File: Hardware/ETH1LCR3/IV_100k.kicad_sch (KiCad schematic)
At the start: 16 parts, among them Q901 BSS123, U1203 AQY221R2S, U901 AD8099ARDZ, U902 AQY221R2S

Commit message: PCB layout
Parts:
- C903: value DNP -> 1p; now fitted; now in the parts list
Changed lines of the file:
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@@
 		(unit 1)
 		(exclude_from_sim no)
-		(in_bom no)
+		(in_bom yes)
 		(on_board yes)
-		(dnp yes)
+		(dnp no)
 		(fields_autoplaced yes)
 		(property "Reference" "C903"
@@
 			)
 		)
-		(property "Value" "DNP"
+		(property "Value" "1p"
 			(at 143.51 63.5 90)
 			(effects

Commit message: PCB layout
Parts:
- added Q1202: MMBT3904, Package_TO_SOT_SMD:SOT-23, symbol Transistor_BJT:MMBT3904
- added R1207: 10k, Resistor_SMD:R_0603_1608Metric_Pad0.98x0.95mm_HandSolder, symbol Device:R
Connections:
- net GND: now also Q1202.2 (E)
- net SW4: now also R1207.2; no longer R903.1, U1203.2
- new net: Q1202.1 (B), R1207.1
- new net _SW4: Q1202.3 (C), R903.1, U1203.2
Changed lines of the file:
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@@
 		)
 	)
-	(label "SW4"
+	(label "_SW4"
 		(at 208.28 85.09 0)
 		(fields_autoplaced yes)
@@
 		)
 	)
-	(label "SW4"
+	(label "_SW4"
 		(at 111.76 111.76 0)
 		(fields_autoplaced yes)
@@
 	(hierarchical_label "SW4"
 		(shape input)
-		(at 215.9 85.09 0)
+		(at 220.98 69.85 90)
 		(fields_autoplaced yes)
 		(effects
@@
 	)
 	(symbol
+		(lib_id "Device:R")
+		(at 220.98 73.66 180)
+		(unit 1)
+		(exclude_from_sim no)
+		(in_bom yes)
+		(on_board yes)
+		(dnp no)
+		(property "Reference" "R1207"
+			(at 215.9 73.66 90)
+			(effects
+				(font
+					(size 1.27 1.27)
+				)
+			)
+		)
+		(property "Value" "10k"
+			(at 218.44 73.66 90)
+			(effects
+				(font
+					(size 1.27 1.27)
+				)
+			)
+		)
+		(property "Footprint" "Resistor_SMD:R_0603_1608Metric_Pad0.98x0.95mm_HandSolder"
+			(at 222.758 73.66 90)
+			(effects
+				(font
+					(size 1.27 1.27)
+				)
+				(hide yes)
+			)
+		)
+		(property "Datasheet" "~"
+			(at 220.98 73.66 0)
+			(effects
+				(font
+					(size 1.27 1.27)
+				)
+				(hide yes)
+			)
+		)
+		(property "Description" "Resistor"
+			(at 220.98 73.66 0)
+			(effects
+				(font
+					(size 1.27 1.27)
+				)
+				(hide yes)
+			)
+		)
+		(pin "1"
+		)
+		(pin "2"
+		)
+		(instances
+			(project "ETH1LCR3"
+				(path "/6623bacb-57aa-43ce-9e51-b38a560dd9fc/37965f22-1055-43ab-ab57-7d9b27fac2d0/3e63d325-b751-4193-9f6f-1795fa7b594f"
+					(reference "R1207")
+					(unit 1)
+				)
+			)
+		)
+	)
+	(symbol
 		(lib_id "power:GND")
 		(at 170.18 68.58 90)
@@
 	(symbol
 		(lib_id "power:GND")
+		(at 226.06 85.09 90)
+		(unit 1)
+		(exclude_from_sim no)
+		(in_bom yes)
+		(on_board yes)
+		(dnp no)
+		(fields_autoplaced yes)
+		(property "Reference" "#PWR01214"
+			(at 232.41 85.09 0)
+			(effects
+				(font
+					(size 1.27 1.27)
+				)
+				(hide yes)
+			)
+		)
+		(property "Value" "GND"
+			(at 229.87 85.0899 90)
+			(effects
+				(font
+					(size 1.27 1.27)
+				)
+				(justify right)
+			)
+		)
+		(property "Footprint" ""
+			(at 226.06 85.09 0)
+			(effects
+				(font
+					(size 1.27 1.27)
+				)
+				(hide yes)
+			)
+		)
+		(property "Datasheet" ""
+			(at 226.06 85.09 0)
+			(effects
+				(font
+					(size 1.27 1.27)
+				)
+				(hide yes)
+			)
+		)
+		(property "Description" "Power symbol creates a global label with name \"GND\" , ground"
+			(at 226.06 85.09 0)
+			(effects
+				(font
+					(size 1.27 1.27)
+				)
+				(hide yes)
+			)
+		)
+		(pin "1"
+		)
+		(instances
+			(project "ETH1LCR3"
+				(path "/6623bacb-57aa-43ce-9e51-b38a560dd9fc/37965f22-1055-43ab-ab57-7d9b27fac2d0/3e63d325-b751-4193-9f6f-1795fa7b594f"
+					(reference "#PWR01214")
+					(unit 1)
+				)
+			)
+		)
+	)
+	(symbol
+		(lib_id "power:GND")
 		(at 142.24 184.15 0)
 		(unit 1)
@@
 					(unit 1)
 				)
+			)
+		)
+	)
+	(symbol
+		(lib_id "Transistor_BJT:MMBT3904")
+		(at 220.98 82.55 90)
+		(mirror x)
+		(unit 1)
+		(exclude_from_sim no)
+		(in_bom yes)
+		(on_board yes)
+		(dnp no)
+		(property "Reference" "Q1202"
+			(at 227.584 77.216 90)
+			(effects
+				(font
+					(size 1.27 1.27)
+				)
+			)
+		)
+		(property "Value" "MMBT3904"
+			(at 227.584 79.756 90)
+			(effects
+				(font
+					(size 1.27 1.27)
+				)
+			)
+		)
+		(property "Footprint" "Package_TO_SOT_SMD:SOT-23"
+			(at 222.885 87.63 0)
+			(effects
+				(font
+					(size 1.27 1.27)
+					(italic yes)
+				)
+				(justify left)
+				(hide yes)
+			)
+		)
+		(property "Datasheet" "https://www.onsemi.com/pdf/datasheet/pzt3904-d.pdf"
+			(at 220.98 82.55 0)
+			(effects
+				(font
+					(size 1.27 1.27)
+				)
+				(justify left)
+				(hide yes)
+			)
+		)
+		(property "Description" "0.2A Ic, 40V Vce, Small Signal NPN Transistor, SOT-23"
+			(at 220.98 82.55 0)
+			(effects
+				(font
+					(size 1.27 1.27)
+				)
+				(hide yes)
+			)
+		)
+		(pin "3"
+		)
+		(pin "2"
+		)
+		(pin "1"
+		)
+		(instances
+			(project "ETH1LCR3"
+				(path "/6623bacb-57aa-43ce-9e51-b38a560dd9fc/37965f22-1055-43ab-ab57-7d9b27fac2d0/3e63d325-b751-4193-9f6f-1795fa7b594f"
+					(reference "Q1202")
+					(unit 1)
+				)

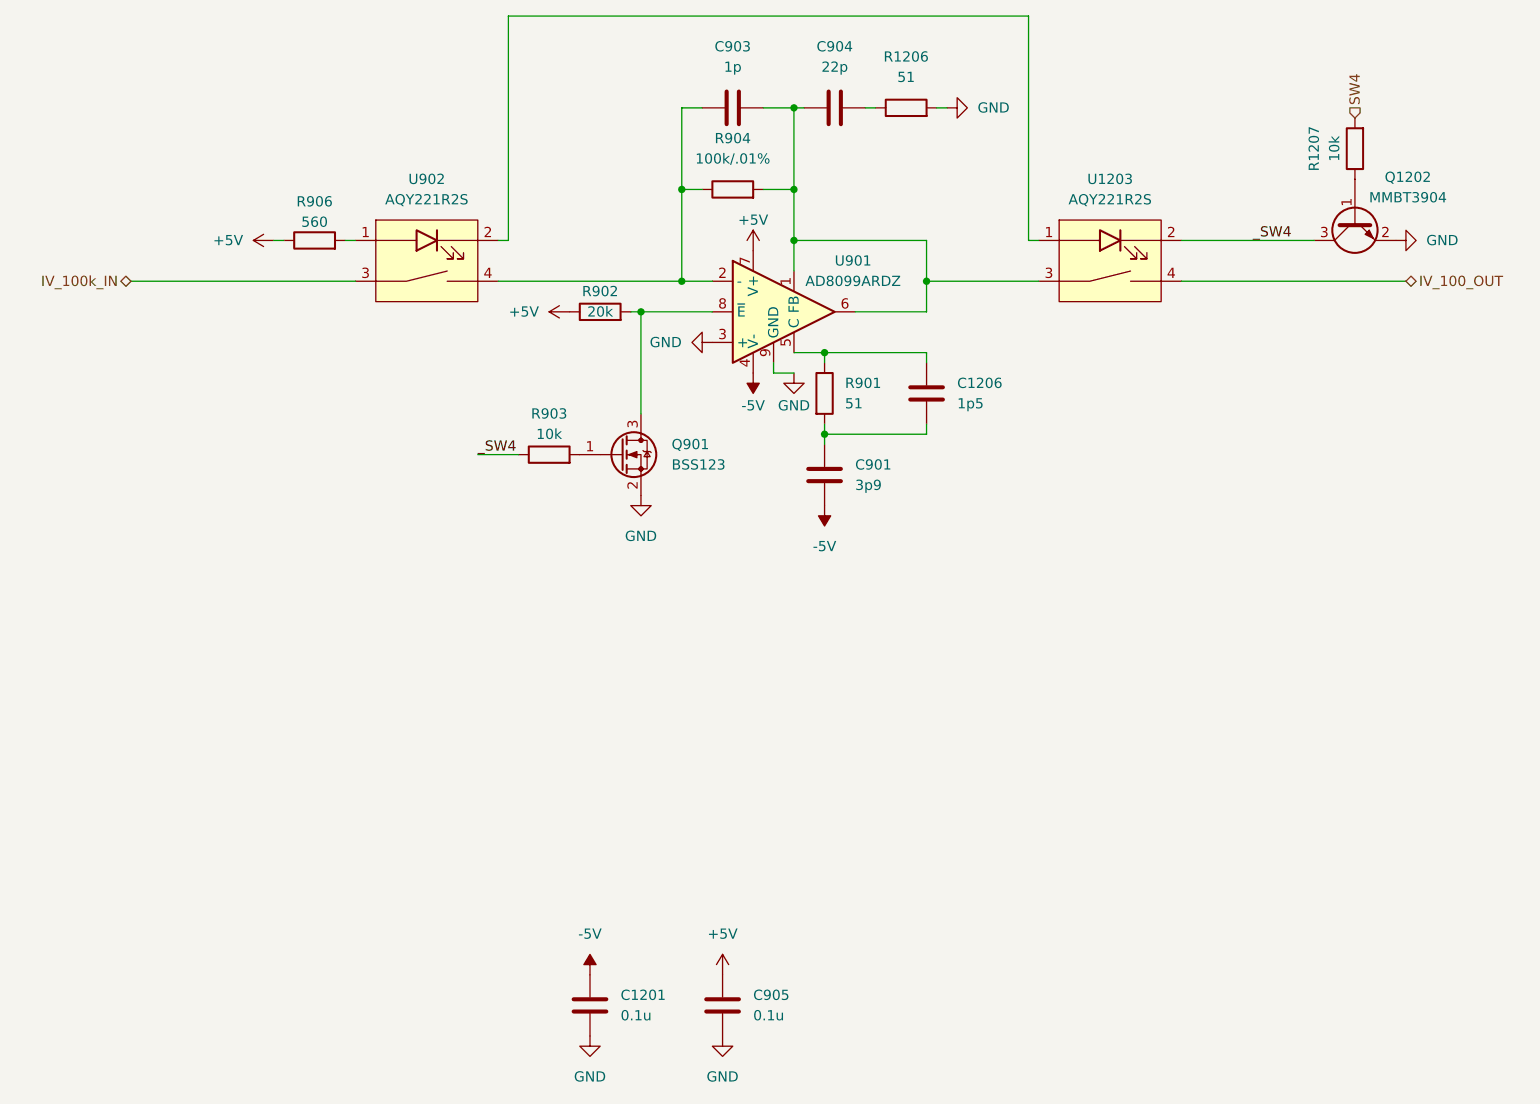
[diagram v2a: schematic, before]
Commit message: Updated project to KiCAD 9
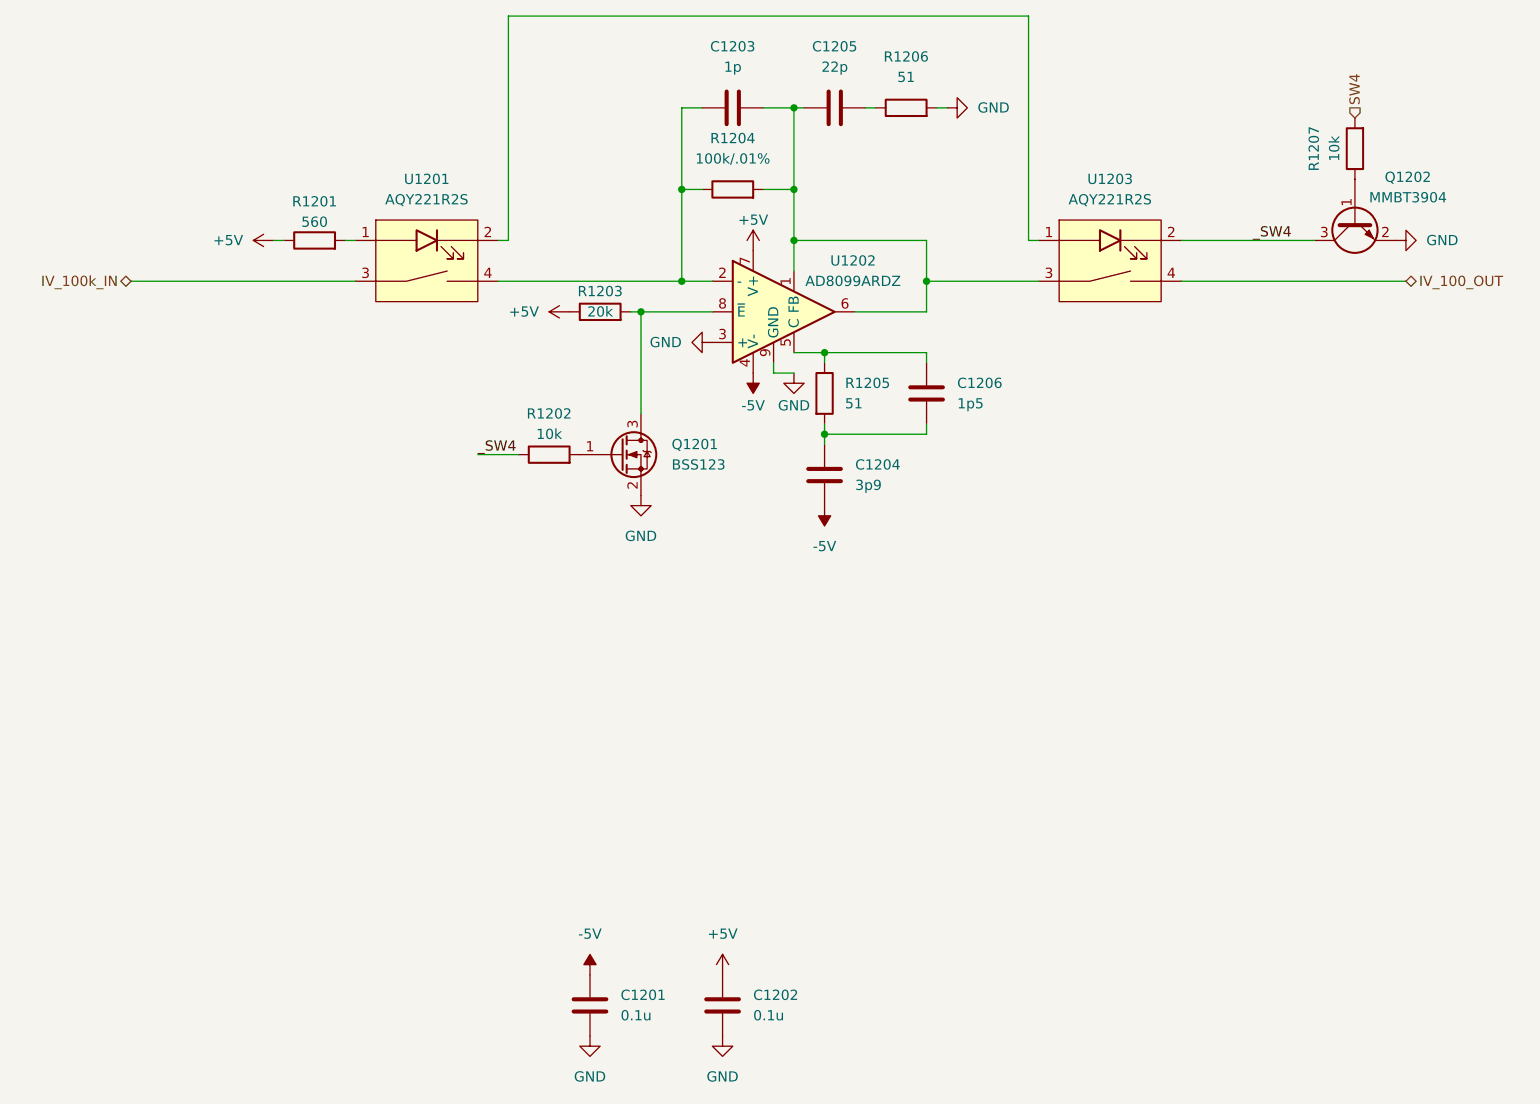
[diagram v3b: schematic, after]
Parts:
- renumbered C905 to C1202, C903 to C1203, C901 to C1204, C904 to C1205, Q901 to Q1201, R906 to R1201, R903 to R1202, R902 to R1203, R904 to R1204, R901 to R1205, U902 to U1201, U901 to U1202
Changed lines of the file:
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@@
 (kicad_sch
-	(version 20231120)
+	(version 20250114)
 	(generator "eeschema")
-	(generator_version "8.0")
+	(generator_version "9.0")
 	(paper "A4")
 	(junction
@@
 	(label "_SW4"
 		(at 208.28 85.09 0)
-		(fields_autoplaced yes)
 		(effects
 			(font
@@
 	(label "_SW4"
 		(at 111.76 111.76 0)
-		(fields_autoplaced yes)
 		(effects
 			(font
@@
 		(shape bidirectional)
 		(at 227.33 90.17 0)
-		(fields_autoplaced yes)
 		(effects
 			(font
@@
 		(shape input)
 		(at 220.98 69.85 90)
-		(fields_autoplaced yes)
 		(effects
 			(font
@@
 		(shape bidirectional)
 		(at 68.58 90.17 180)
-		(fields_autoplaced yes)
 		(effects
 			(font
@@
 		(dnp no)
 		(fields_autoplaced yes)
-		(property "Reference" "#PWR0904"
+		(property "Reference" "#PWR01202"
 			(at 127 93.98 0)
 			(effects
@@
 		(dnp no)
 		(fields_autoplaced yes)
-		(property "Reference" "#PWR0907"
+		(property "Reference" "#PWR01213"
 			(at 176.53 68.58 0)
 			(effects
@@
 		(dnp no)
 		(fields_autoplaced yes)
-		(property "Reference" "#PWR0901"
+		(property "Reference" "#PWR01212"
 			(at 154.94 114.3 0)
 			(effects
@@
 		(dnp no)
 		(fields_autoplaced yes)
-		(property "Reference" "C903"
+		(property "Reference" "C1203"
 			(at 143.51 60.96 90)
 			(effects
@@
 		(on_board yes)
 		(dnp no)
-		(property "Reference" "U901"
+		(property "Reference" "U1202"
 			(at 158.496 87.63 0)
 			(effects
@@
 		(on_board yes)
 		(dnp no)
-		(property "Reference" "C901"
+		(property "Reference" "C1204"
 			(at 158.75 113.0299 0)
 			(effects
@@
 		(on_board yes)
 		(dnp no)
-		(property "Reference" "R903"
+		(property "Reference" "R1202"
 			(at 120.65 106.68 90)
 			(effects
@@
 		(on_board yes)
 		(dnp no)
-		(property "Reference" "R906"
+		(property "Reference" "R1201"
 			(at 91.44 80.264 90)
 			(effects
@@
 		(dnp no)
 		(fields_autoplaced yes)
-		(property "Reference" "#PWR0902"
+		(property "Reference" "#PWR01206"
 			(at 134.62 97.79 0)
 			(effects
@@
 		(dnp no)
 		(fields_autoplaced yes)
-		(property "Reference" "R904"
+		(property "Reference" "R1204"
 			(at 143.51 72.39 90)
 			(effects
@@
 		(on_board yes)
 		(dnp no)
-		(property "Reference" "R902"
+		(property "Reference" "R1203"
 			(at 127 91.44 90)
 			(effects
@@
 		(dnp no)
 		(fields_autoplaced yes)
-		(property "Reference" "C905"
+		(property "Reference" "C1202"
 			(at 146.05 179.0699 0)
 			(effects
@@
 		(dnp no)
 		(fields_autoplaced yes)
-		(property "Reference" "R901"
+		(property "Reference" "R1205"
 			(at 157.48 102.8699 0)
 			(effects
@@
 		(on_board yes)
 		(dnp no)
-		(property "Reference" "#PWR0905"
+		(property "Reference" "#PWR01209"
 			(at 146.05 90.17 0)
 			(effects
@@
 		(dnp no)
 		(fields_autoplaced yes)
-		(property "Reference" "C904"
+		(property "Reference" "C1205"
 			(at 156.21 60.96 90)
 			(effects
@@
 		(dnp no)
 		(fields_autoplaced yes)
-		(property "Reference" "Q901"
+		(property "Reference" "Q1201"
 			(at 135.89 110.4899 0)
 			(effects
@@
 		(dnp no)
 		(fields_autoplaced yes)
-		(property "Reference" "#PWR0908"
+		(property "Reference" "#PWR01201"
 			(at 90.17 85.09 0)
 			(effects
@@
 		(dnp no)
 		(fields_autoplaced yes)
-		(property "Reference" "U902"
+		(property "Reference" "U1201"
 			(at 105.41 77.47 0)
 			(effects
@@
 		(on_board yes)
 		(dnp no)
-		(property "Reference" "#PWR0906"
+		(property "Reference" "#PWR01210"
 			(at 146.05 97.79 0)
 			(effects
